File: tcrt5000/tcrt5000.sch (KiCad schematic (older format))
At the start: 7 parts, among them Q1 BC817, U1 TCRT5000, X1 Conn_01x03_Male

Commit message: Gerbers done
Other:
- moved on the sheet: Q1, R1, R2, R3, R4, U1, X1
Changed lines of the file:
@@
 L tcrt5000:TCRT5000 U1
 U 1 1 5E29CC7F
-P 3925 2425
-F 0 "U1" H 4153 2491 50  0000 L CNN
-F 1 "TCRT5000" H 4153 2400 50  0000 L CNN
-F 2 "tcrt5000:TCRT500" H 4153 2309 50  0000 L CNN
-F 3 "" H 3925 2375 50  0001 C CNN
-	1    3925 2425
+P 4650 3550
+F 0 "U1" H 4878 3616 50  0000 L CNN
+F 1 "TCRT5000" H 4878 3525 50  0000 L CNN
+F 2 "tcrt5000:TCRT500" H 4878 3434 50  0000 L CNN
+F 3 "" H 4650 3500 50  0001 C CNN
+	1    4650 3550
 	1    0    0    -1
 $EndComp
 Wire Wire Line
-	3825 2125 3825 1825
+	4550 3250 4550 2950
 Wire Wire Line
-	3825 1825 4025 1825
+	4550 2950 4750 2950
 Wire Wire Line
-	4025 2125 4025 1825
-Connection ~ 4025 1825
+	4750 3250 4750 2950
+Connection ~ 4750 2950
 $Comp
 L Device:R R2
 U 1 1 5E29DACB
-P 4025 3325
-F 0 "R2" H 4095 3371 50  0000 L CNN
-F 1 "330R" H 4095 3280 50  0000 L CNN
-F 2 "Resistor_SMD:R_0805_2012Metric" V 3955 3325 50  0001 C CNN
-F 3 "~" H 4025 3325 50  0001 C CNN
-	1    4025 3325
+P 4750 4450
+F 0 "R2" H 4820 4496 50  0000 L CNN
+F 1 "330R" H 4820 4405 50  0000 L CNN
+F 2 "Resistor_SMD:R_0805_2012Metric" V 4680 4450 50  0001 C CNN
+F 3 "~" H 4750 4450 50  0001 C CNN
+	1    4750 4450
 	1    0    0    -1
 $EndComp
@@
 L Device:R R1
 U 1 1 5E29DF88
-P 3825 3325
-F 0 "R1" H 3895 3371 50  0000 L CNN
-F 1 "10K" H 3895 3280 50  0000 L CNN
-F 2 "Resistor_SMD:R_0805_2012Metric" V 3755 3325 50  0001 C CNN
-F 3 "~" H 3825 3325 50  0001 C CNN
-	1    3825 3325
+P 4550 4450
+F 0 "R1" H 4350 4500 50  0000 L CNN
+F 1 "10K" H 4325 4400 50  0000 L CNN
+F 2 "Resistor_SMD:R_0805_2012Metric" V 4480 4450 50  0001 C CNN
+F 3 "~" H 4550 4450 50  0001 C CNN
+	1    4550 4450
 	1    0    0    -1
 $EndComp
 Wire Wire Line
-	3825 3475 3825 3600
+	4550 4600 4550 4725
 Wire Wire Line
-	3825 3600 4025 3600
+	4550 4725 4750 4725
 Wire Wire Line
-	4025 3475 4025 3600
-Connection ~ 4025 3600
+	4750 4600 4750 4725
+Connection ~ 4750 4725
 Wire Wire Line
-	3825 3175 3825 2975
+	4550 4300 4550 4100
 Wire Wire Line
-	4025 2775 4025 3175
+	4750 3900 4750 4300
 Wire Wire Line
-	3825 2975 4300 2975
-Connection ~ 3825 2975
+	4550 4100 5025 4100
+Connection ~ 4550 4100
 Wire Wire Line
-	3825 2975 3825 2775
+	4550 4100 4550 3900
 $Comp
 L Device:R R3
 U 1 1 5E29E5DC
-P 4450 2975
-F 0 "R3" V 4243 2975 50  0000 C CNN
-F 1 "10K" V 4334 2975 50  0000 C CNN
-F 2 "Resistor_SMD:R_0805_2012Metric" V 4380 2975 50  0001 C CNN
-F 3 "~" H 4450 2975 50  0001 C CNN
-	1    4450 2975
+P 5175 4100
+F 0 "R3" V 4968 4100 50  0000 C CNN
+F 1 "10K" V 5059 4100 50  0000 C CNN
+F 2 "Resistor_SMD:R_0805_2012Metric" V 5105 4100 50  0001 C CNN
+F 3 "~" H 5175 4100 50  0001 C CNN
+	1    5175 4100
 	0    1    1    0
 $EndComp
 Wire Wire Line
-	4600 2975 4900 2975
+	5325 4100 5375 4100
 $Comp
 L Transistor_BJT:BC817 Q1
 U 1 1 5E29F24F
-P 5100 2975
-F 0 "Q1" H 5291 3021 50  0000 L CNN
-F 1 "BC817" H 5291 2930 50  0000 L CNN
-F 2 "Package_TO_SOT_SMD:SOT-23" H 5300 2900 50  0001 L CIN
-F 3 "http://www.fairchildsemi.com/ds/BC/BC817.pdf" H 5100 2975 50  0001 L CNN
-	1    5100 2975
+P 5575 4100
+F 0 "Q1" H 5766 4146 50  0000 L CNN
+F 1 "BC817" H 5766 4055 50  0000 L CNN
+F 2 "Package_TO_SOT_SMD:SOT-23" H 5775 4025 50  0001 L CIN
+F 3 "http://www.fairchildsemi.com/ds/BC/BC817.pdf" H 5575 4100 50  0001 L CNN
+	1    5575 4100
 	1    0    0    -1
 $EndComp
 Wire Wire Line
-	5200 3175 5200 3600
+	5675 4300 5675 4725
 Wire Wire Line
-	4025 3600 5200 3600
+	4750 4725 5675 4725
 $Comp
 L Device:R R4
 U 1 1 5E29FB00
-P 5200 2350
-F 0 "R4" H 5270 2396 50  0000 L CNN
-F 1 "10K" H 5270 2305 50  0000 L CNN
-F 2 "Resistor_SMD:R_0805_2012Metric" V 5130 2350 50  0001 C CNN
-F 3 "~" H 5200 2350 50  0001 C CNN
-	1    5200 2350
+P 5675 3375
+F 0 "R4" H 5745 3421 50  0000 L CNN
+F 1 "10K" H 5745 3330 50  0000 L CNN
+F 2 "Resistor_SMD:R_0805_2012Metric" V 5605 3375 50  0001 C CNN
+F 3 "~" H 5675 3375 50  0001 C CNN
+	1    5675 3375
 	1    0    0    -1
 $EndComp
 Wire Wire Line
-	5200 2500 5200 2600
+	5675 3525 5675 3725
 Wire Wire Line
-	5200 2200 5200 1825
+	5675 3225 5675 2950
 Wire Wire Line
-	4025 1825 5200 1825
-Connection ~ 5200 1825
-Connection ~ 5200 2600
+	4750 2950 5675 2950
+Connection ~ 5675 2950
+Connection ~ 5675 3725
 Wire Wire Line
-	5200 2600 5200 2775
-Connection ~ 5200 3600
+	5675 3725 5675 3900
+Connection ~ 5675 4725
 $Comp
 L Connector:Conn_01x03_Male X1
 U 1 1 5E2A6981
-P 6625 2600
-F 0 "X1" H 6597 2624 50  0000 R CNN
-F 1 "Conn_01x03_Male" H 6597 2533 50  0000 R CNN
-F 2 "Connector_PinHeader_2.54mm:PinHeader_1x03_P2.54mm_Vertical" H 6625 2600 50  0001 C CNN
-F 3 "~" H 6625 2600 50  0001 C CNN
-	1    6625 2600
+P 7100 3725
+F 0 "X1" H 7072 3749 50  0000 R CNN
+F 1 "Conn_01x03_Male" H 7072 3658 50  0000 R CNN
+F 2 "Connector_PinHeader_2.54mm:PinHeader_1x03_P2.54mm_Vertical" H 7100 3725 50  0001 C CNN
+F 3 "~" H 7100 3725 50  0001 C CNN
+	1    7100 3725
 	-1   0    0    -1
 $EndComp
-Text Label 5925 1825 2    50   ~ 0
+Text Label 6400 2950 2    50   ~ 0
 VCC
-Text Label 5950 2600 2    50   ~ 0
+Text Label 6425 3725 2    50   ~ 0
 OUT
-Text Label 6000 3600 2    50   ~ 0
+Text Label 6475 4725 2    50   ~ 0
 GND
 Wire Wire Line
-	6150 1825 6150 2500
+	6625 2950 6625 3625
 Wire Wire Line
-	6150 2500 6425 2500
+	6625 3625 6900 3625
 Wire Wire Line
-	5200 1825 6150 1825
+	5675 2950 6625 2950
 Wire Wire Line
-	5200 2600 6425 2600
+	5675 3725 6900 3725
 Wire Wire Line
-	6150 3600 6150 2700
+	6625 4725 6625 3825
 Wire Wire Line
-	6150 2700 6425 2700
+	6625 3825 6900 3825
 Wire Wire Line
-	5200 3600 6150 3600
+	5675 4725 6625 4725
 $EndSCHEMATC

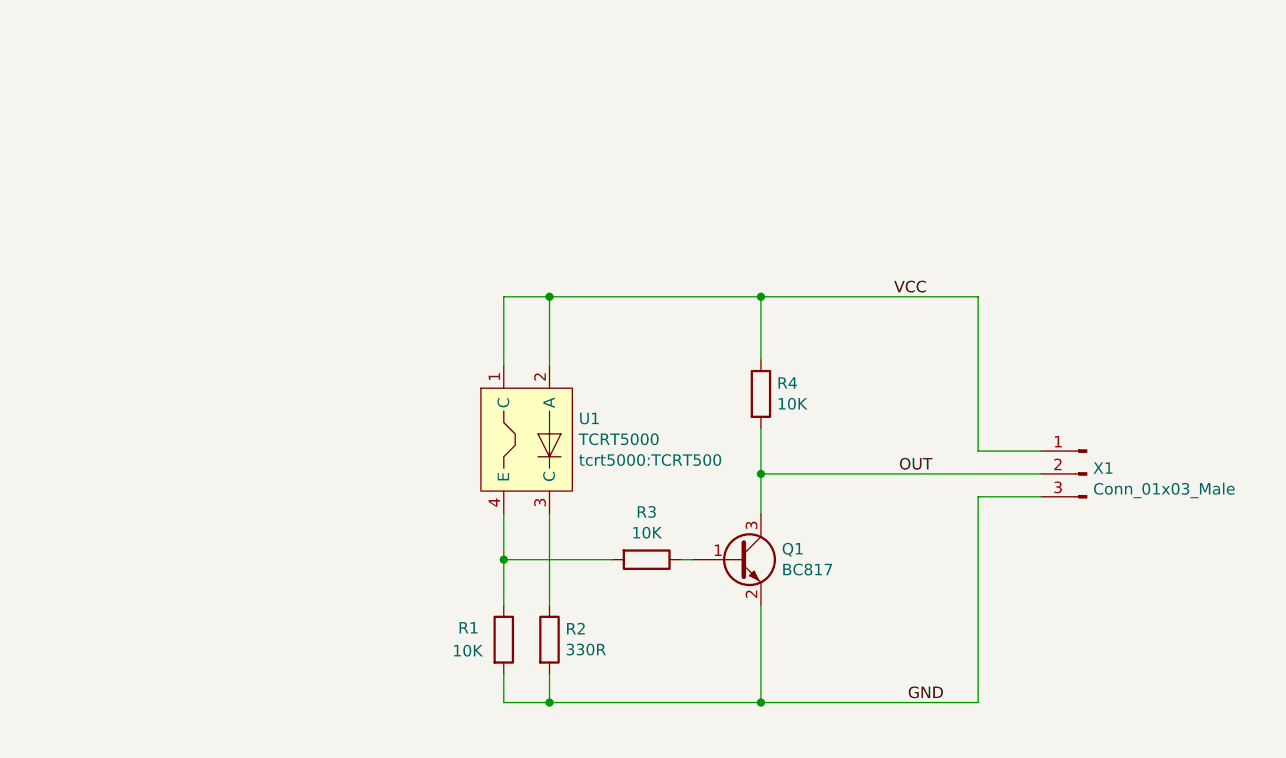
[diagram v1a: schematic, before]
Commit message: LED resistor calculations added
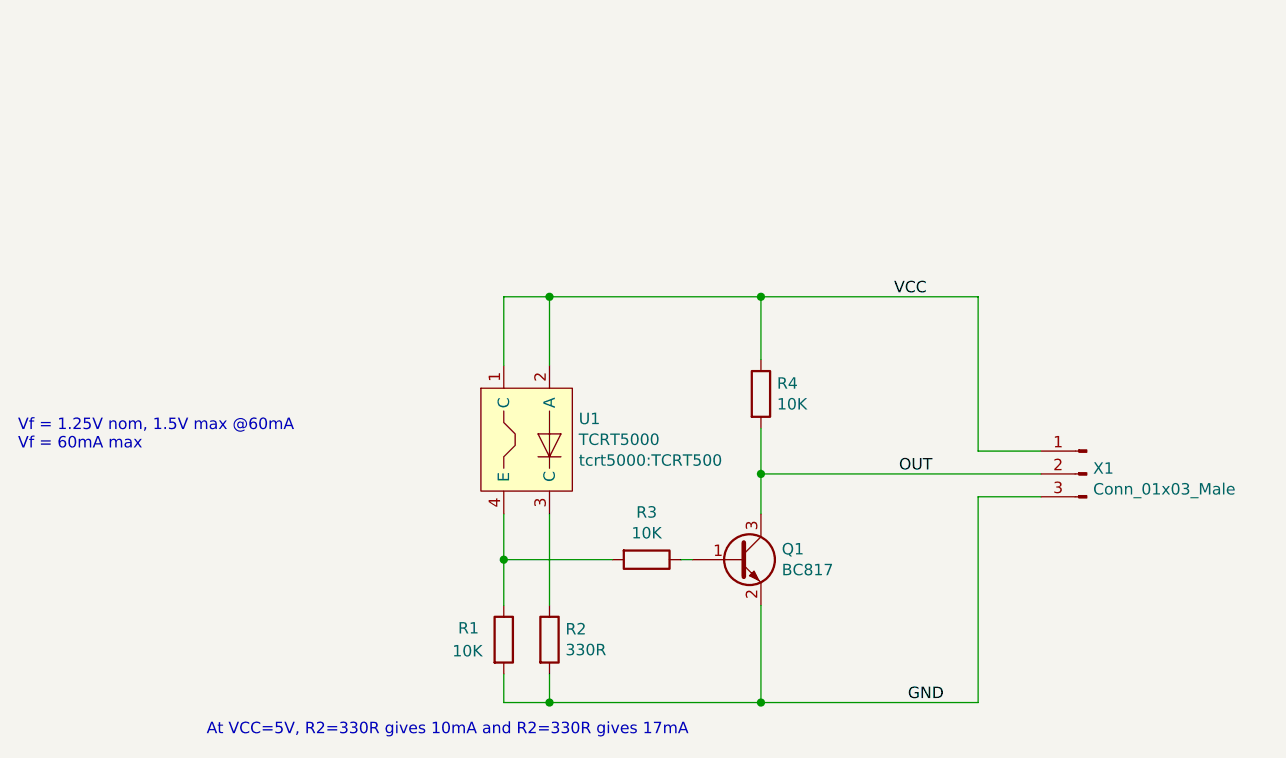
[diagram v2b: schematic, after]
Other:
- note added: "At VCC=5V, R2=330R gives 10mA and R2=330R gives 17mA"
- note added: "Vf = 1.25V nom, 1.5V max @60mA\nVf = 60mA max\n"
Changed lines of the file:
@@
 Wire Wire Line
 	5675 4725 6625 4725
+Text Notes 2425 3625 0    50   ~ 0
+Vf = 1.25V nom, 1.5V max @60mA\nVf = 60mA max\n
+Text Notes 3250 4875 0    50   ~ 0
+At VCC=5V, R2=330R gives 10mA and R2=330R gives 17mA
 $EndSCHEMATC
